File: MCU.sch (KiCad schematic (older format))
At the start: 10 parts, among them U2 TPS70925, U3 STM32L011F4Ux

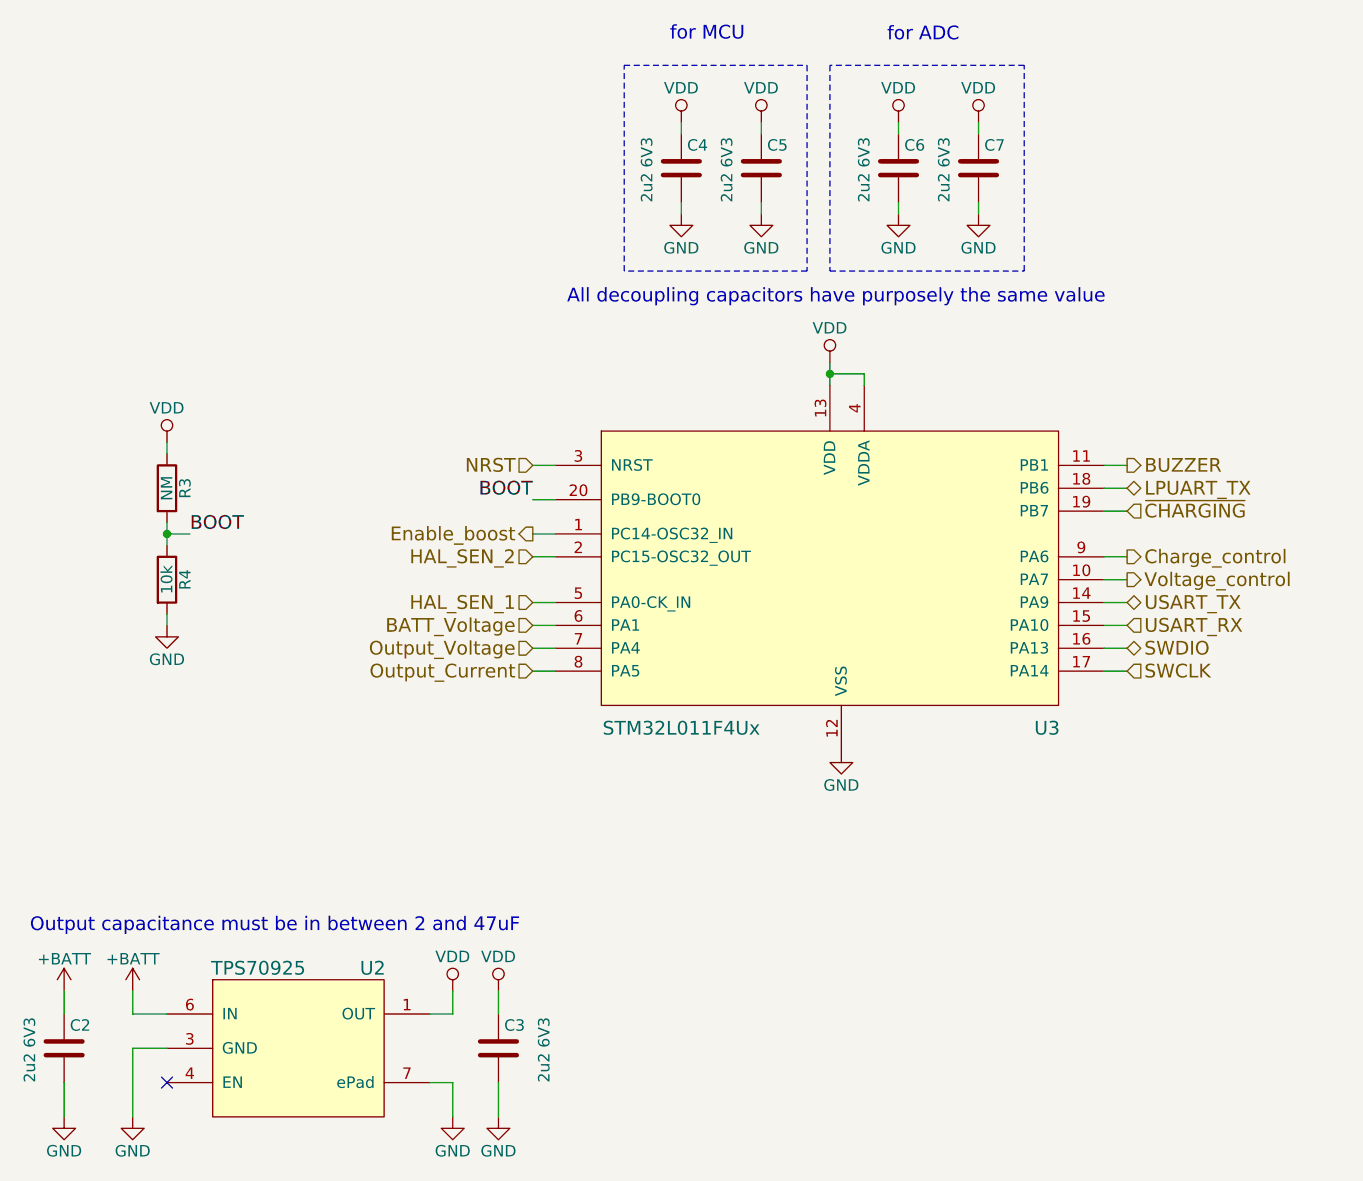
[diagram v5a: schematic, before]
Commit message: Removed boost converter, added output switch
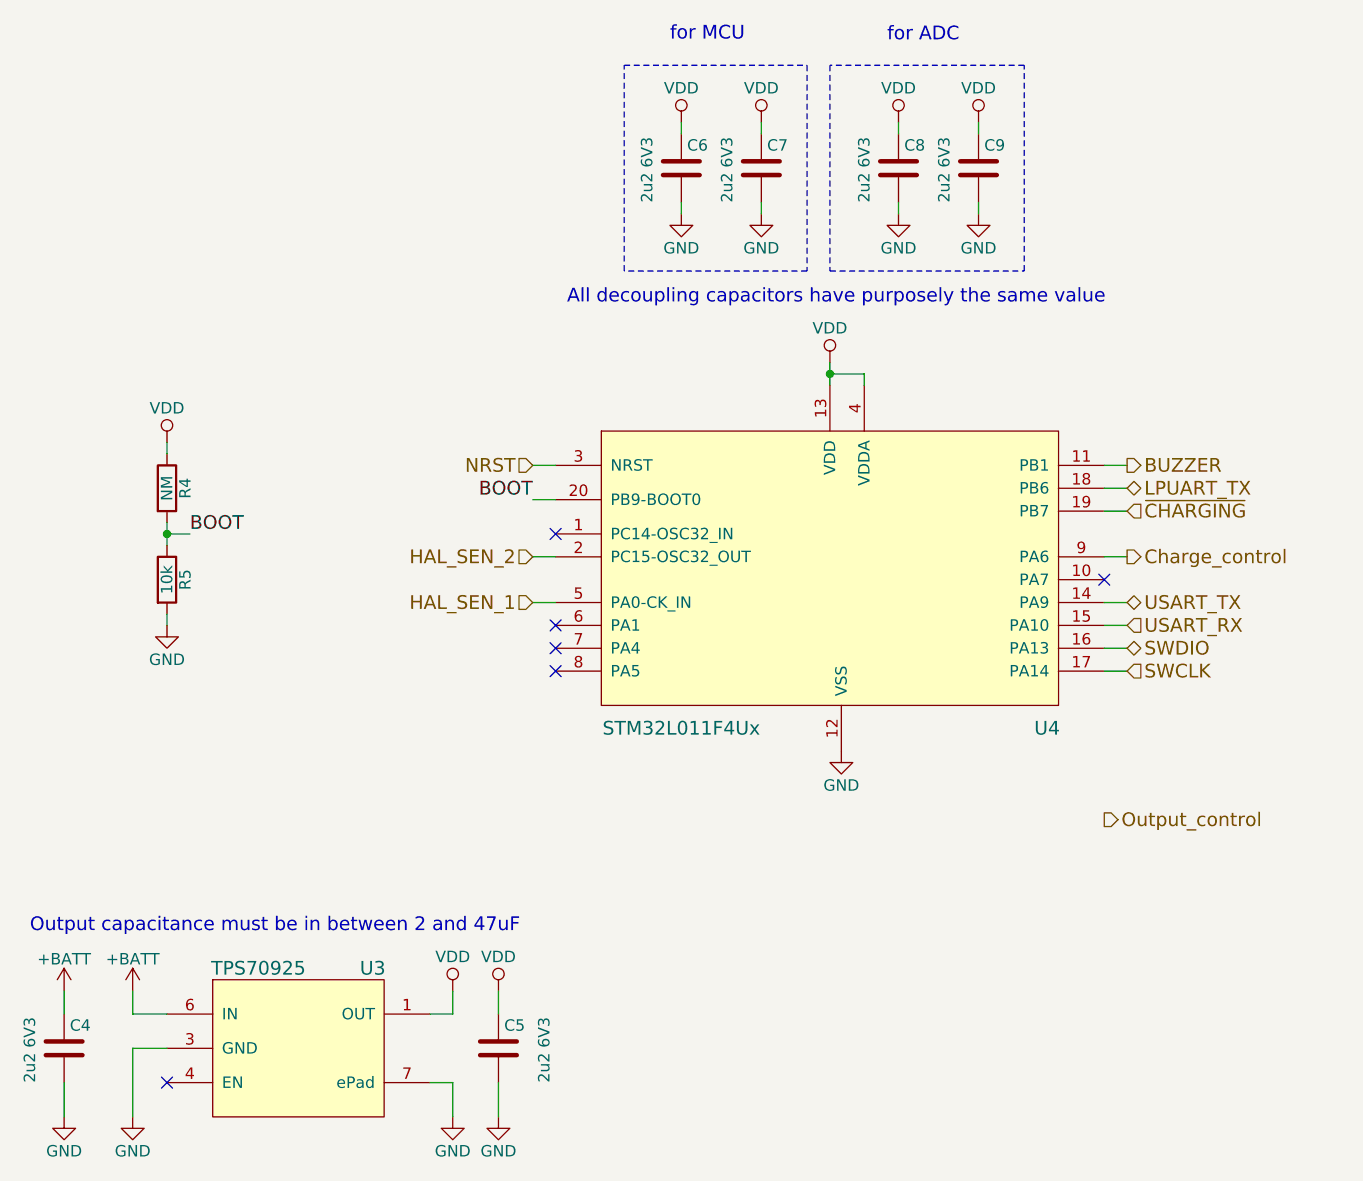
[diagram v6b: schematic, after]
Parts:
- renumbered C2 to C4, C3 to C5, C4 to C6, C5 to C7, C6 to C8, C7 to C9, R3 to R4, R4 to R5, U2 to U3, U3 to U4
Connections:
- net BATT_Voltage: no longer names the net of U4.6 (PA1)
- net Enable_boost: no longer names the net of U4.1 (PC14-OSC32_IN)
- net Output_Current: no longer names the net of U4.8 (PA5)
- net Output_Voltage: no longer names the net of U4.7 (PA4)
- net Voltage_control: no longer names the net of U4.10 (PA7)
- no-connect marks 1 -> 6
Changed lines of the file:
@@
 LIBS:Transistor
 LIBS:Connector
+LIBS:lakotamm-loadswitch
 LIBS:F3K_Battery_manager-cache
 EELAYER 25 0
@@
 $Descr A4 11693 8268
 encoding utf-8
-Sheet 2 4
+Sheet 2 3
 Title ""
 Date ""
@@
 $EndDescr
 $Comp
-L VDD #PWR012
+L VDD #PWR31
 U 1 1 5A9B30A9
 P 6100 3250
-F 0 "#PWR012" H 6100 3100 50  0001 C CNN
+F 0 "#PWR31" H 6100 3100 50  0001 C CNN
 F 1 "VDD" H 6100 3400 50  0000 C CNN
 F 2 "" H 6100 3250 50  0001 C CNN
@@
 Connection ~ 6100 3300
 $Comp
-L GND #PWR013
+L GND #PWR32
 U 1 1 5A9B30B3
 P 6150 4950
-F 0 "#PWR013" H 6150 4700 50  0001 C CNN
+F 0 "#PWR32" H 6150 4700 50  0001 C CNN
 F 1 "GND" H 6150 4800 50  0000 C CNN
 F 2 "" H 6150 4950 50  0001 C CNN
@@
 $EndComp
 $Comp
-L GND #PWR014
+L GND #PWR20
 U 1 1 5A9B3148
 P 3050 6550
-F 0 "#PWR014" H 3050 6300 50  0001 C CNN
+F 0 "#PWR20" H 3050 6300 50  0001 C CNN
 F 1 "GND" H 3050 6400 50  0000 C CNN
 F 2 "" H 3050 6550 50  0001 C CNN
@@
 NoConn ~ 3200 6400
 $Comp
-L GND #PWR015
+L GND #PWR24
 U 1 1 5A9B3188
 P 4450 6550
-F 0 "#PWR015" H 4450 6300 50  0001 C CNN
+F 0 "#PWR24" H 4450 6300 50  0001 C CNN
 F 1 "GND" H 4450 6400 50  0000 C CNN
 F 2 "" H 4450 6550 50  0001 C CNN
@@
 	4450 6400 4450 6550
 $Comp
-L VDD #PWR016
+L VDD #PWR23
 U 1 1 5A9B31B3
 P 4450 6000
-F 0 "#PWR016" H 4450 5850 50  0001 C CNN
+F 0 "#PWR23" H 4450 5850 50  0001 C CNN
 F 1 "VDD" H 4450 6150 50  0000 C CNN
 F 2 "" H 4450 6000 50  0001 C CNN
@@
 	4450 6100 4350 6100
 $Comp
-L +BATT #PWR017
+L +BATT #PWR19
 U 1 1 5A9B31F8
 P 3050 6000
-F 0 "#PWR017" H 3050 5850 50  0001 C CNN
+F 0 "#PWR19" H 3050 5850 50  0001 C CNN
 F 1 "+BATT" H 3050 6140 50  0000 C CNN
 F 2 "" H 3050 6000 50  0001 C CNN
@@
 	3050 6100 3200 6100
 $Comp
-L C C3
+L C C5
 U 1 1 5A9B323D
 P 4650 6250
-F 0 "C3" H 4675 6350 50  0000 L CNN
+F 0 "C5" H 4675 6350 50  0000 L CNN
 F 1 "2u2 6V3" V 4850 6100 50  0000 L CNN
 F 2 "Capacitors_SMD:C_0402" H 4688 6100 50  0001 C CNN
@@
 $EndComp
 $Comp
-L VDD #PWR018
+L VDD #PWR25
 U 1 1 5A9B32A8
 P 4650 6000
-F 0 "#PWR018" H 4650 5850 50  0001 C CNN
+F 0 "#PWR25" H 4650 5850 50  0001 C CNN
 F 1 "VDD" H 4650 6150 50  0000 C CNN
 F 2 "" H 4650 6000 50  0001 C CNN
@@
 $EndComp
 $Comp
-L GND #PWR019
+L GND #PWR26
 U 1 1 5A9B32D5
 P 4650 6550
-F 0 "#PWR019" H 4650 6300 50  0001 C CNN
+F 0 "#PWR26" H 4650 6300 50  0001 C CNN
 F 1 "GND" H 4650 6400 50  0000 C CNN
 F 2 "" H 4650 6550 50  0001 C CNN
@@
 	4650 6400 4650 6550
 $Comp
-L C C2
+L C C4
 U 1 1 5A9B33BC
 P 2750 6250
-F 0 "C2" H 2775 6350 50  0000 L CNN
+F 0 "C4" H 2775 6350 50  0000 L CNN
 F 1 "2u2 6V3" V 2600 6100 50  0000 L CNN
 F 2 "Capacitors_SMD:C_0402" H 2788 6100 50  0001 C CNN
@@
 $EndComp
 $Comp
-L GND #PWR020
+L GND #PWR18
 U 1 1 5A9B33C8
 P 2750 6550
-F 0 "#PWR020" H 2750 6300 50  0001 C CNN
+F 0 "#PWR18" H 2750 6300 50  0001 C CNN
 F 1 "GND" H 2750 6400 50  0000 C CNN
 F 2 "" H 2750 6550 50  0001 C CNN
@@
 	2750 6400 2750 6550
 $Comp
-L +BATT #PWR021
+L +BATT #PWR17
 U 1 1 5A9B33E9
 P 2750 6000
-F 0 "#PWR021" H 2750 5850 50  0001 C CNN
+F 0 "#PWR17" H 2750 5850 50  0001 C CNN
 F 1 "+BATT" H 2750 6140 50  0000 C CNN
 F 2 "" H 2750 6000 50  0001 C CNN
@@
 $EndComp
 $Comp
-L C C4
+L C C6
 U 1 1 5A9B3893
 P 5450 2400
-F 0 "C4" H 5475 2500 50  0000 L CNN
+F 0 "C6" H 5475 2500 50  0000 L CNN
 F 1 "2u2 6V3" V 5300 2250 50  0000 L CNN
 F 2 "Capacitors_SMD:C_0402" H 5488 2250 50  0001 C CNN
@@
 Output capacitance must be in between 2 and 47uF\n
 $Comp
-L VDD #PWR022
+L VDD #PWR27
 U 1 1 5A9B3944
 P 5450 2200
-F 0 "#PWR022" H 5450 2050 50  0001 C CNN
+F 0 "#PWR27" H 5450 2050 50  0001 C CNN
 F 1 "VDD" H 5450 2350 50  0000 C CNN
 F 2 "" H 5450 2200 50  0001 C CNN
@@
 	5450 2200 5450 2250
 $Comp
-L GND #PWR023
+L GND #PWR28
 U 1 1 5A9B3984
 P 5450 2600
-F 0 "#PWR023" H 5450 2350 50  0001 C CNN
+F 0 "#PWR28" H 5450 2350 50  0001 C CNN
 F 1 "GND" H 5450 2450 50  0000 C CNN
 F 2 "" H 5450 2600 50  0001 C CNN
@@
 	5450 2550 5450 2600
 $Comp
-L C C5
+L C C7
 U 1 1 5A9B39ED
 P 5800 2400
-F 0 "C5" H 5825 2500 50  0000 L CNN
+F 0 "C7" H 5825 2500 50  0000 L CNN
 F 1 "2u2 6V3" V 5650 2250 50  0000 L CNN
 F 2 "Capacitors_SMD:C_0402" H 5838 2250 50  0001 C CNN
@@
 $EndComp
 $Comp
-L VDD #PWR024
+L VDD #PWR29
 U 1 1 5A9B39F3
 P 5800 2200
-F 0 "#PWR024" H 5800 2050 50  0001 C CNN
+F 0 "#PWR29" H 5800 2050 50  0001 C CNN
 F 1 "VDD" H 5800 2350 50  0000 C CNN
 F 2 "" H 5800 2200 50  0001 C CNN
@@
 	5800 2200 5800 2250
 $Comp
-L GND #PWR025
+L GND #PWR30
 U 1 1 5A9B39FA
 P 5800 2600
-F 0 "#PWR025" H 5800 2350 50  0001 C CNN
+F 0 "#PWR30" H 5800 2350 50  0001 C CNN
 F 1 "GND" H 5800 2450 50  0000 C CNN
 F 2 "" H 5800 2600 50  0001 C CNN
@@
 	5800 2550 5800 2600
 $Comp
-L C C6
+L C C8
 U 1 1 5A9B3B25
 P 6400 2400
-F 0 "C6" H 6425 2500 50  0000 L CNN
+F 0 "C8" H 6425 2500 50  0000 L CNN
 F 1 "2u2 6V3" V 6250 2250 50  0000 L CNN
 F 2 "Capacitors_SMD:C_0402" H 6438 2250 50  0001 C CNN
@@
 $EndComp
 $Comp
-L VDD #PWR026
+L VDD #PWR33
 U 1 1 5A9B3B2B
 P 6400 2200
-F 0 "#PWR026" H 6400 2050 50  0001 C CNN
+F 0 "#PWR33" H 6400 2050 50  0001 C CNN
 F 1 "VDD" H 6400 2350 50  0000 C CNN
 F 2 "" H 6400 2200 50  0001 C CNN
@@
 	6400 2200 6400 2250
 $Comp
-L GND #PWR027
+L GND #PWR34
 U 1 1 5A9B3B32
 P 6400 2600
-F 0 "#PWR027" H 6400 2350 50  0001 C CNN
+F 0 "#PWR34" H 6400 2350 50  0001 C CNN
 F 1 "GND" H 6400 2450 50  0000 C CNN
 F 2 "" H 6400 2600 50  0001 C CNN
@@
 	6400 2550 6400 2600
 $Comp
-L C C7
+L C C9
 U 1 1 5A9B3B84
 P 6750 2400
-F 0 "C7" H 6775 2500 50  0000 L CNN
+F 0 "C9" H 6775 2500 50  0000 L CNN
 F 1 "2u2 6V3" V 6600 2250 50  0000 L CNN
 F 2 "Capacitors_SMD:C_0402" H 6788 2250 50  0001 C CNN
@@
 $EndComp
 $Comp
-L VDD #PWR028
+L VDD #PWR35
 U 1 1 5A9B3B8A
 P 6750 2200
-F 0 "#PWR028" H 6750 2050 50  0001 C CNN
+F 0 "#PWR35" H 6750 2050 50  0001 C CNN
 F 1 "VDD" H 6750 2350 50  0000 C CNN
 F 2 "" H 6750 2200 50  0001 C CNN
@@
 	6750 2200 6750 2250
 $Comp
-L GND #PWR029
+L GND #PWR36
 U 1 1 5A9B3B91
 P 6750 2600
-F 0 "#PWR029" H 6750 2350 50  0001 C CNN
+F 0 "#PWR36" H 6750 2350 50  0001 C CNN
 F 1 "GND" H 6750 2450 50  0000 C CNN
 F 2 "" H 6750 2600 50  0001 C CNN
@@
 	7300 4500 7400 4500
 $Comp
-L R R4
+L R R5
 U 1 1 5A9B431F
 P 3200 4200
-F 0 "R4" V 3280 4200 50  0000 C CNN
+F 0 "R5" V 3280 4200 50  0000 C CNN
 F 1 "10k" V 3200 4200 50  0000 C CNN
 F 2 "Resistors_SMD:R_0402" V 3130 4200 50  0001 C CNN
@@
 $EndComp
 $Comp
-L R R3
+L R R4
 U 1 1 5A9B4434
 P 3200 3800
-F 0 "R3" V 3280 3800 50  0000 C CNN
+F 0 "R4" V 3280 3800 50  0000 C CNN
 F 1 "NM" V 3200 3800 50  0000 C CNN
 F 2 "Resistors_SMD:R_0402" V 3130 3800 50  0001 C CNN
@@
 $EndComp
 $Comp
-L VDD #PWR030
+L VDD #PWR21
 U 1 1 5A9B4476
 P 3200 3600
-F 0 "#PWR030" H 3200 3450 50  0001 C CNN
+F 0 "#PWR21" H 3200 3450 50  0001 C CNN
 F 1 "VDD" H 3200 3750 50  0000 C CNN
 F 2 "" H 3200 3600 50  0001 C CNN
@@
 	3200 3650 3200 3600
 $Comp
-L GND #PWR031
+L GND #PWR22
 U 1 1 5A9B4528
 P 3200 4400
-F 0 "#PWR031" H 3200 4150 50  0001 C CNN
+F 0 "#PWR22" H 3200 4150 50  0001 C CNN
 F 1 "GND" H 3200 4250 50  0000 C CNN
 F 2 "" H 3200 4400 50  0001 C CNN
@@
 Text HLabel 7400 3700 2    60   Output ~ 0
 BUZZER
-Text HLabel 7400 4200 2    60   Output ~ 0
-Voltage_control
-Text HLabel 4800 4000 0    60   Output ~ 0
-Enable_boost
-Wire Wire Line
-	4800 4400 4900 4400
-Text HLabel 4800 4400 0    60   Input ~ 0
-BATT_Voltage
 Wire Wire Line
 	7300 3700 7400 3700
 Wire Wire Line
 	7300 4100 7400 4100
-Wire Wire Line
-	4800 4000 4900 4000
-$Comp
-L TPS709 U2
+$Comp
+L TPS709 U3
 U 1 1 5AA7A66F
 P 3800 6250
-F 0 "U2" H 4100 6600 60  0000 C CNN
+F 0 "U3" H 4100 6600 60  0000 C CNN
 F 1 "TPS70925" H 3600 6600 60  0000 C CNN
 F 2 "lakotamm-miscellaneous:WSON-6_2x2mm_Pitch0.65mm" H 3850 5600 60  0001 C CNN
@@
 Charge_control
 Wire Wire Line
-	7300 4200 7400 4200
-Wire Wire Line
 	4900 4100 4800 4100
 Wire Wire Line
@@
 	7300 3800 7400 3800
 $Comp
-L STM32L011F4Ux U3
+L STM32L011F4Ux U4
 U 1 1 5AA7A3A1
 P 6150 4200
-F 0 "U3" H 7050 3550 60  0000 C CNN
+F 0 "U4" H 7050 3550 60  0000 C CNN
 F 1 "STM32L011F4Ux" H 5450 3550 60  0000 C CNN
 F 2 "Housings_DFN_QFN:ST_UFQFPN-20_3x3mm_Pitch0.5mm" H 6150 3300 60  0001 C CNN
@@
 	1    0    0    -1
 $EndComp
-Text HLabel 4800 4500 0    60   Input ~ 0
-Output_Voltage
-Text HLabel 4800 4600 0    60   Input ~ 0
-Output_Current
-Wire Wire Line
-	4800 4600 4900 4600
-Wire Wire Line
-	4800 4500 4900 4500
+NoConn ~ 4900 4400
+NoConn ~ 4900 4500
+NoConn ~ 4900 4600
+NoConn ~ 4900 4000
+NoConn ~ 7300 4200
+Text HLabel 7300 5250 2    60   Output ~ 0
+Output_control
 $EndSCHEMATC
